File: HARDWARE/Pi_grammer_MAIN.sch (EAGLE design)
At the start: 31 parts, among them J2 TARGET_copy, J3 TESTBED, J4 CABLE, U1 AT42QT1010SOT23

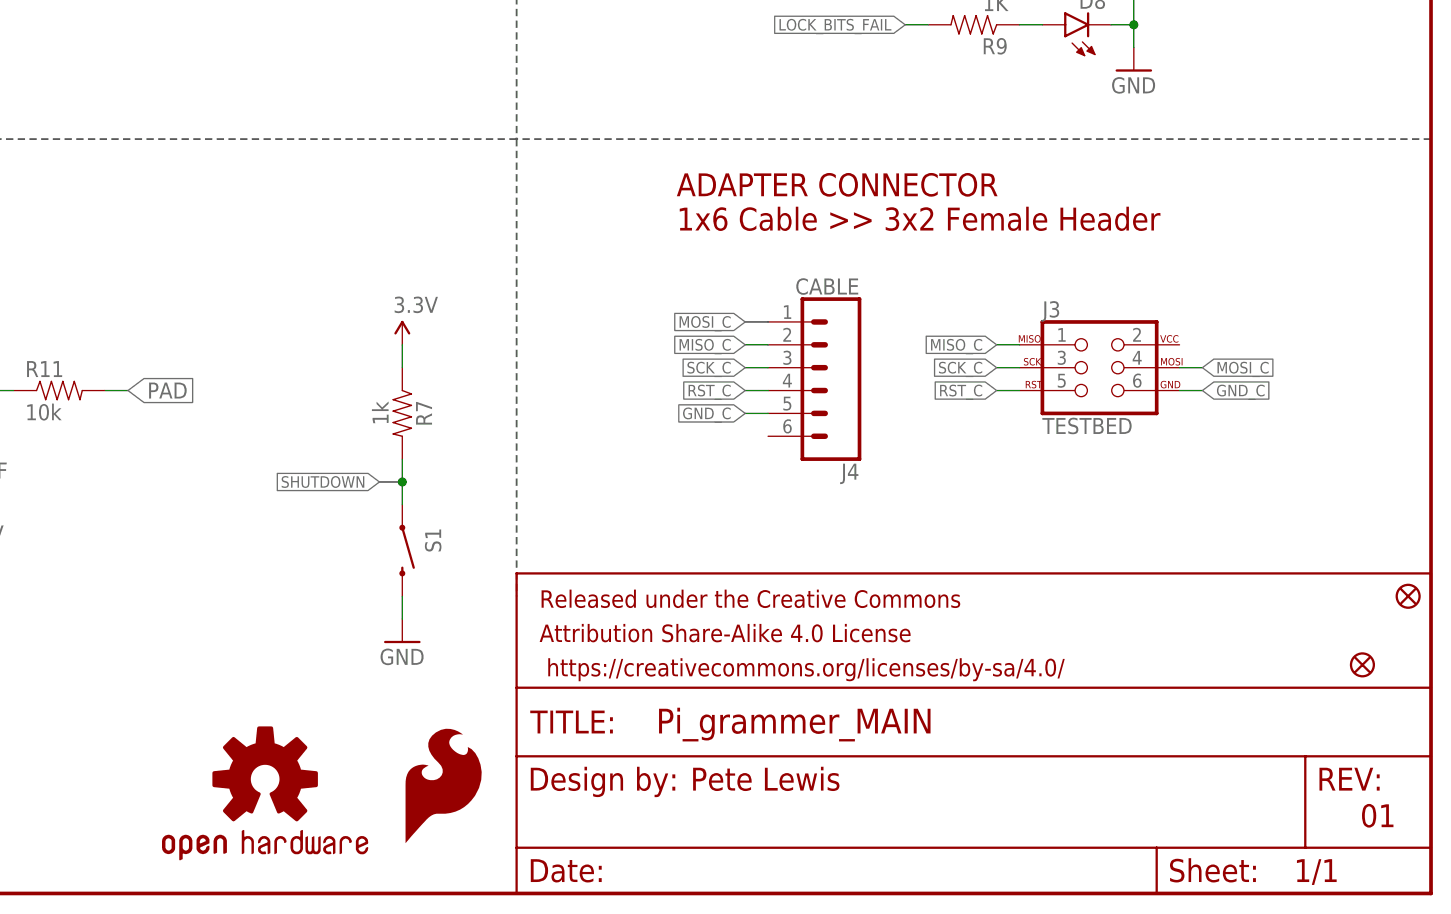
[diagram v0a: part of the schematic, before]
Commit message: Split design into MAIN and ADAPTER
The original eagle file contained both PCBs for this project. As
requested by production, I split them out into separate design files -
for ease of CAMing and ordering.
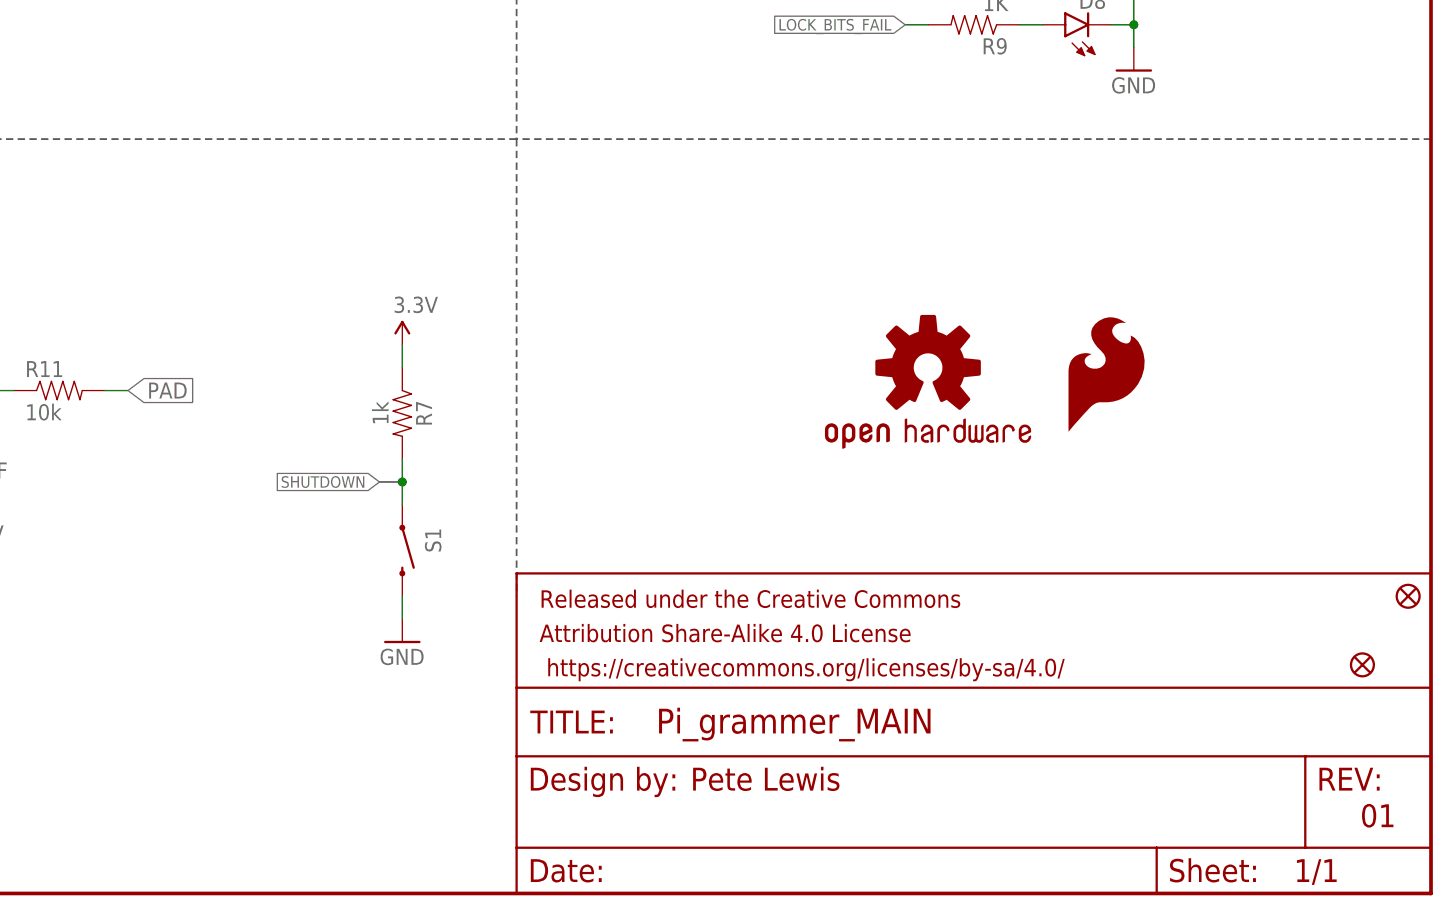
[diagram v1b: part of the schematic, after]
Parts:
- removed J3: TESTBED, SparkFun-Connectors:AVR_SPI_PROG_3X22X3_LOCK
- removed J4: CABLE, SparkFun-Connectors:CONN_06RA
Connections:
- removed net GND_C: J3.6, J4.5
- removed net MISO_C: J3.1, J4.2
- removed net MOSI_C: J3.4, J4.1
- removed net RST_C: J3.5, J4.4
- removed net SCK_C: J3.3, J4.3
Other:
- note removed: "ADAPTER CONNECTOR 1x6 Cable >> 3x2 Female Header"
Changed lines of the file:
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@@
 </part>
 <part name="GND6" library="SparkFun-Aesthetics" deviceset="GND" device=""/>
-<part name="J3" library="SparkFun-Connectors" deviceset="AVR_SPI_PROG_3X2" device="2X3_LOCK" value="TESTBED">
-<attribute name="PROD_ID" value="CONN-11566"/>
-</part>
-<part name="J4" library="SparkFun-Connectors" deviceset="CONN_06" device="RA" value="CABLE">
-<attribute name="PROD_ID" value="CONN-10140"/>
-</part>
 <part name="FRAME1" library="SparkFun-Aesthetics" deviceset="FRAME-LETTER" device=""/>
 <part name="FD1" library="SparkFun-Aesthetics" deviceset="FIDUCIAL" device="UFIDUCIAL"/>
@@
 <plain>
 <wire x1="256.54" y1="266.7" x2="154.94" y2="266.7" width="0.2032" layer="97" style="shortdash"/>
-<text x="172.72" y="256.54" size="2.54" layer="94" font="vector">ADAPTER CONNECTOR
-1x6 Cable &gt;&gt; 3x2 Female Header</text>
 <wire x1="154.94" y1="266.7" x2="154.94" y2="215.9" width="0.2032" layer="97" style="shortdash"/>
 <wire x1="154.94" y1="368.3" x2="154.94" y2="266.7" width="0.2032" layer="97" style="shortdash"/>
@@
 <instance part="R8" gate="G$1" x="205.74" y="289.56" rot="R180"/>
 <instance part="D7" gate="G$1" x="215.9" y="289.56" rot="R90"/>
-<instance part="LOGO1" gate="G$1" x="142.24" y="187.96"/>
-<instance part="LOGO2" gate="G$1" x="127" y="195.58"/>
+<instance part="LOGO1" gate="G$1" x="215.9" y="233.68"/>
+<instance part="LOGO2" gate="G$1" x="200.66" y="241.3"/>
 <instance part="U1" gate="G$1" x="63.5" y="226.06">
 <attribute name="PROD_ID" x="63.5" y="226.06" size="1.27" layer="96" display="off"/>
@@
 </instance>
 <instance part="GND6" gate="1" x="124.46" y="307.34"/>
-<instance part="J3" gate="G$1" x="218.44" y="241.3">
-<attribute name="PROD_ID" x="218.44" y="241.3" size="1.27" layer="96" display="off"/>
-</instance>
-<instance part="J4" gate="G$1" x="187.96" y="241.3" rot="R180">
-<attribute name="PROD_ID" x="187.96" y="241.3" size="1.27" layer="96" rot="R180" display="off"/>
-</instance>
 <instance part="FRAME1" gate="G$1" x="7.62" y="182.88"/>
 <instance part="FRAME1" gate="V" x="154.94" y="182.88"/>
@@
 </segment>
 </net>
-<net name="MOSI_C" class="0">
-<segment>
-<pinref part="J4" gate="G$1" pin="1"/>
-<wire x1="182.88" y1="246.38" x2="180.34" y2="246.38" width="0.1524" layer="91"/>
-<label x="180.34" y="246.38" size="1.27" layer="95" rot="R180" xref="yes"/>
-</segment>
-<segment>
-<pinref part="J3" gate="G$1" pin="4"/>
-<wire x1="228.6" y1="241.3" x2="231.14" y2="241.3" width="0.1524" layer="91"/>
-<label x="231.14" y="241.3" size="1.27" layer="95" xref="yes"/>
-</segment>
-</net>
-<net name="MISO_C" class="0">
-<segment>
-<pinref part="J4" gate="G$1" pin="2"/>
-<wire x1="182.88" y1="243.84" x2="180.34" y2="243.84" width="0.1524" layer="91"/>
-<label x="180.34" y="243.84" size="1.27" layer="95" rot="R180" xref="yes"/>
-</segment>
-<segment>
-<pinref part="J3" gate="G$1" pin="1"/>
-<wire x1="210.82" y1="243.84" x2="208.28" y2="243.84" width="0.1524" layer="91"/>
-<label x="208.28" y="243.84" size="1.27" layer="95" rot="R180" xref="yes"/>
-</segment>
-</net>
-<net name="SCK_C" class="0">
-<segment>
-<pinref part="J3" gate="G$1" pin="3"/>
-<wire x1="210.82" y1="241.3" x2="208.28" y2="241.3" width="0.1524" layer="91"/>
-<label x="208.28" y="241.3" size="1.27" layer="95" rot="R180" xref="yes"/>
-</segment>
-<segment>
-<pinref part="J4" gate="G$1" pin="3"/>
-<wire x1="182.88" y1="241.3" x2="180.34" y2="241.3" width="0.1524" layer="91"/>
-<label x="180.34" y="241.3" size="1.27" layer="95" rot="R180" xref="yes"/>
-</segment>
-</net>
-<net name="RST_C" class="0">
-<segment>
-<pinref part="J4" gate="G$1" pin="4"/>
-<wire x1="182.88" y1="238.76" x2="180.34" y2="238.76" width="0.1524" layer="91"/>
-<label x="180.34" y="238.76" size="1.27" layer="95" rot="R180" xref="yes"/>
-</segment>
-<segment>
-<pinref part="J3" gate="G$1" pin="5"/>
-<wire x1="210.82" y1="238.76" x2="208.28" y2="238.76" width="0.1524" layer="91"/>
-<label x="208.28" y="238.76" size="1.27" layer="95" rot="R180" xref="yes"/>
-</segment>
-</net>
-<net name="GND_C" class="0">
-<segment>
-<pinref part="J4" gate="G$1" pin="5"/>
-<wire x1="182.88" y1="236.22" x2="180.34" y2="236.22" width="0.1524" layer="91"/>
-<label x="180.34" y="236.22" size="1.27" layer="95" rot="R180" xref="yes"/>
-</segment>
-<segment>
-<pinref part="J3" gate="G$1" pin="6"/>
-<wire x1="228.6" y1="238.76" x2="231.14" y2="238.76" width="0.1524" layer="91"/>
-<label x="231.14" y="238.76" size="1.27" layer="95" xref="yes"/>
-</segment>
-</net>
 </nets>
 </sheet>
@@
 </schematic>
 </drawing>
-<compatibility>
-<note version="6.3" minversion="6.2.2" severity="warning">
-Since Version 6.2.2 text objects can contain more than one line,
-which will not be processed correctly with this version.
-</note>
-</compatibility>
 </eagle>
